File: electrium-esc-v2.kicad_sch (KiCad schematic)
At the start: 5 parts, among them J1 CAN

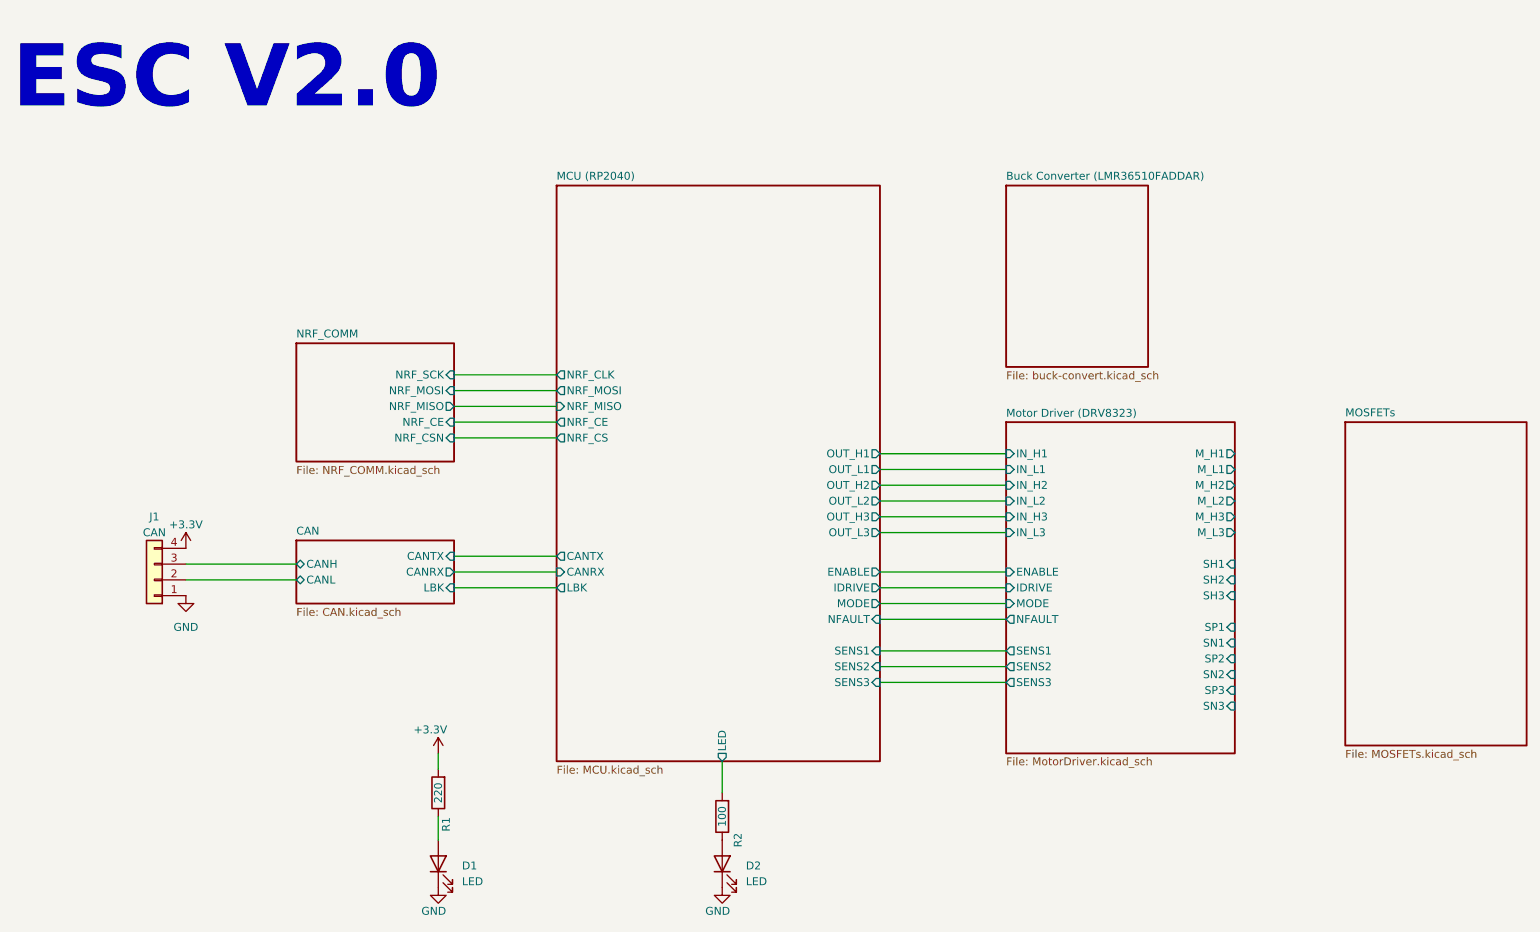
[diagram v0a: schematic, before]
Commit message: changed pins
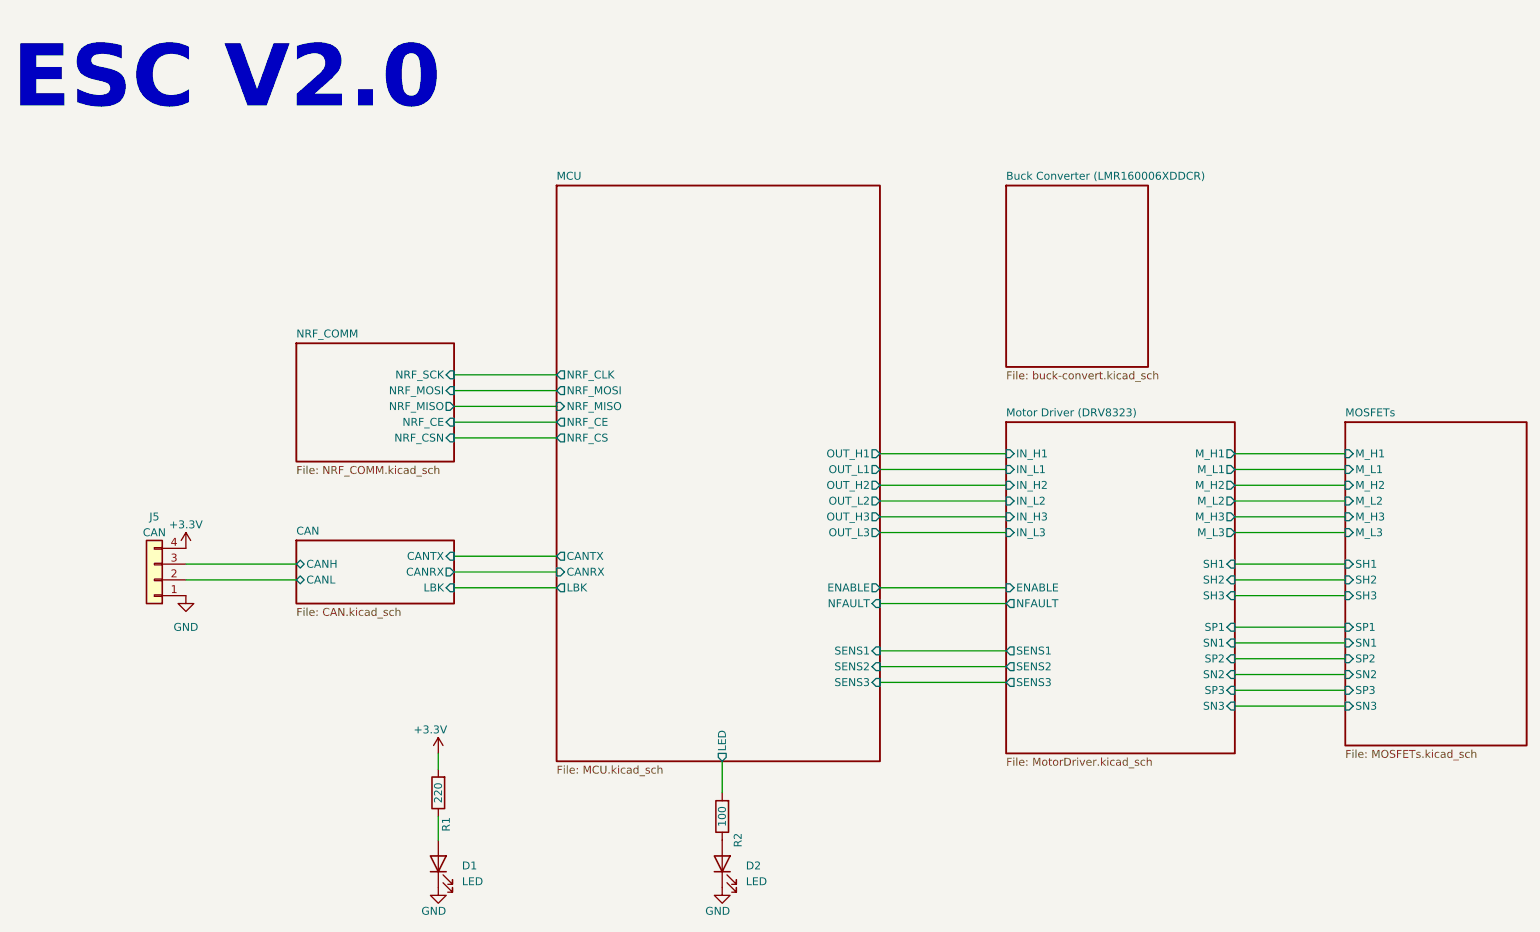
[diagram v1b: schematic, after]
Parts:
- J5: renamed from J1; footprint Connector_JST:JST_XH_B4B-XH-A_1x04_P2.50mm_Vertical -> (none)
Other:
- sheet Buck Converter (LMR36510FADDAR) renamed Buck Converter (LMR160006XDDCR)
- sheet MCU (RP2040) renamed MCU
- sheet MCU ports: added none; removed IDRIVE, MODE
- sheet MOSFETs ports: added M_H1, M_H2, M_H3, M_L1, M_L2, M_L3, SH1, SH2, SH3, SN1, SN2, SN3, SP1, SP2, SP3; removed none
- sheet Motor Driver (DRV8323) ports: added none; removed IDRIVE, MODE

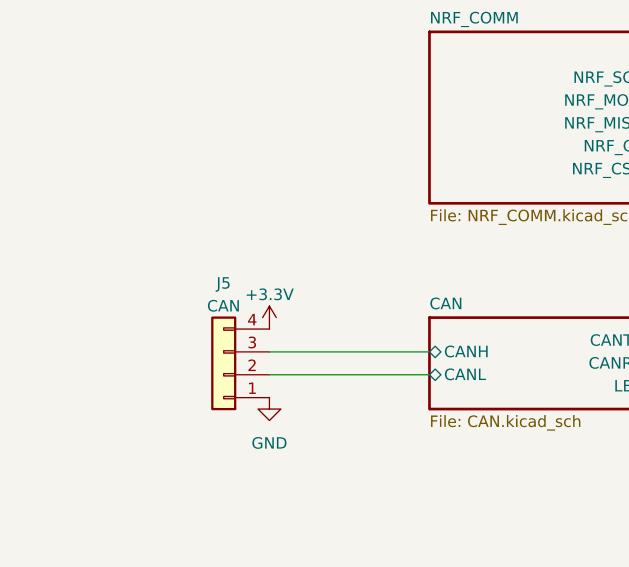
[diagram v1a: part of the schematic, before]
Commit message: Re-annotate all components
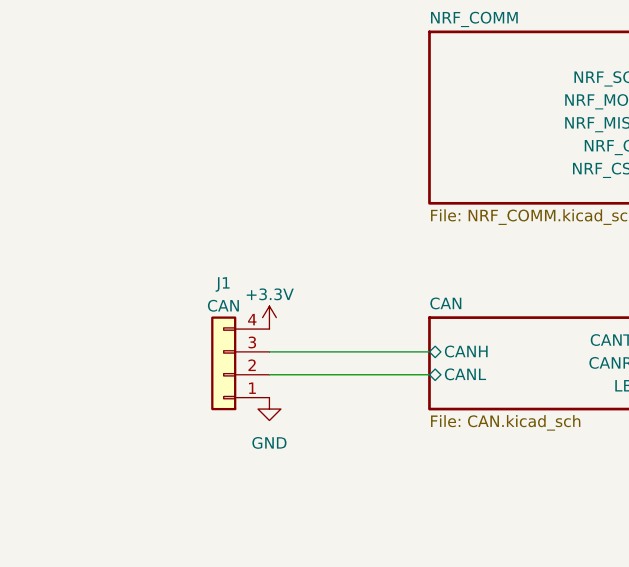
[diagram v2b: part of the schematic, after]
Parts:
- renumbered J5 to J1
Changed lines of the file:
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@@
   (symbol (lib_id "power:GND") (at 134.62 157.48 0) (unit 1)
     (in_bom yes) (on_board yes) (dnp no)
-    (property "Reference" "#PWR06" (at 134.62 163.83 0)
+    (property "Reference" "#PWR059" (at 134.62 163.83 0)
       (effects (font (size 1.27 1.27)) hide)
     )
@@
       (project "electrium-esc-v2"
         (path "/be00c12c-11fa-42cb-8a0b-46fcd24b2ced"
-          (reference "#PWR06") (unit 1)
-        )
-      )
-      (project "electrium-esc"
-        (path "/d277d506-2f4d-497b-a498-1ff059e212d2"
-          (reference "#PWR066") (unit 1)
+          (reference "#PWR059") (unit 1)
+        )
+      )
+      (project "electrium-esc"
+        (path "/d277d506-2f4d-497b-a498-1ff059e212d2"
+          (reference "#PWR?") (unit 1)
         )
       )
@@
   (symbol (lib_id "power:GND") (at 88.9 157.48 0) (unit 1)
     (in_bom yes) (on_board yes) (dnp no)
-    (property "Reference" "#PWR05" (at 88.9 163.83 0)
+    (property "Reference" "#PWR058" (at 88.9 163.83 0)
       (effects (font (size 1.27 1.27)) hide)
     )
@@
       (project "electrium-esc-v2"
         (path "/be00c12c-11fa-42cb-8a0b-46fcd24b2ced"
-          (reference "#PWR05") (unit 1)
-        )
-      )
-      (project "electrium-esc"
-        (path "/d277d506-2f4d-497b-a498-1ff059e212d2"
-          (reference "#PWR065") (unit 1)
+          (reference "#PWR058") (unit 1)
+        )
+      )
+      (project "electrium-esc"
+        (path "/d277d506-2f4d-497b-a498-1ff059e212d2"
+          (reference "#PWR?") (unit 1)
         )
       )
@@
   (symbol (lib_id "power:+3.3V") (at 88.9 135.89 0) (unit 1)
     (in_bom yes) (on_board yes) (dnp no)
-    (property "Reference" "#PWR04" (at 88.9 139.7 0)
+    (property "Reference" "#PWR057" (at 88.9 139.7 0)
       (effects (font (size 1.27 1.27)) hide)
     )
@@
       (project "electrium-esc-v2"
         (path "/be00c12c-11fa-42cb-8a0b-46fcd24b2ced"
-          (reference "#PWR04") (unit 1)
-        )
-      )
-      (project "electrium-esc"
-        (path "/d277d506-2f4d-497b-a498-1ff059e212d2"
-          (reference "#PWR061") (unit 1)
+          (reference "#PWR057") (unit 1)
+        )
+      )
+      (project "electrium-esc"
+        (path "/d277d506-2f4d-497b-a498-1ff059e212d2"
+          (reference "#PWR?") (unit 1)
         )
       )
@@
       (project "electrium-esc"
         (path "/d277d506-2f4d-497b-a498-1ff059e212d2"
-          (reference "D5") (unit 1)
+          (reference "D?") (unit 1)
         )
       )
@@
   (symbol (lib_id "power:+3.3V") (at 48.26 102.87 0) (unit 1)
     (in_bom yes) (on_board yes) (dnp no) (fields_autoplaced)
-    (property "Reference" "#PWR038" (at 48.26 106.68 0)
+    (property "Reference" "#PWR055" (at 48.26 106.68 0)
       (effects (font (size 1.27 1.27)) hide)
     )
@@
       (project "electrium-esc-v2"
         (path "/be00c12c-11fa-42cb-8a0b-46fcd24b2ced"
-          (reference "#PWR038") (unit 1)
+          (reference "#PWR055") (unit 1)
         )
       )
@@
   (symbol (lib_id "power:GND") (at 48.26 110.49 0) (unit 1)
     (in_bom yes) (on_board yes) (dnp no) (fields_autoplaced)
-    (property "Reference" "#PWR039" (at 48.26 116.84 0)
+    (property "Reference" "#PWR056" (at 48.26 116.84 0)
       (effects (font (size 1.27 1.27)) hide)
     )
@@
       (project "electrium-esc-v2"
         (path "/be00c12c-11fa-42cb-8a0b-46fcd24b2ced"
-          (reference "#PWR039") (unit 1)
+          (reference "#PWR056") (unit 1)
         )
       )
@@
   (symbol (lib_id "Connector_Generic:Conn_01x04") (at 43.18 107.95 180) (unit 1)
     (in_bom yes) (on_board yes) (dnp no) (fields_autoplaced)
-    (property "Reference" "J5" (at 43.18 97.79 0)
+    (property "Reference" "J1" (at 43.18 97.79 0)
       (effects (font (size 1.27 1.27)))
     )
@@
       (project "electrium-esc-v2"
         (path "/be00c12c-11fa-42cb-8a0b-46fcd24b2ced"
-          (reference "J5") (unit 1)
+          (reference "J1") (unit 1)
         )
       )
@@
       (project "electrium-esc"
         (path "/d277d506-2f4d-497b-a498-1ff059e212d2"
-          (reference "R66") (unit 1)
+          (reference "R?") (unit 1)
         )
       )
@@
       (project "electrium-esc"
         (path "/d277d506-2f4d-497b-a498-1ff059e212d2"
-          (reference "R65") (unit 1)
+          (reference "R?") (unit 1)
         )
       )
@@
       (project "electrium-esc"
         (path "/d277d506-2f4d-497b-a498-1ff059e212d2"
-          (reference "D6") (unit 1)
-        )
-      )
+          (reference "D?") (unit 1)
+        )
+      )
